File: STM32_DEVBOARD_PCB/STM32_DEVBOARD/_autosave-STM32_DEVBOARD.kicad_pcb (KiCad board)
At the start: 2 copper layers, 49.8 x 40.4 mm, 62 parts, among them J1 Screw_Terminal_01x02, J2 USB_C_Receptacle_USB2.0, J3 SWD, J4 Conn_01x03_Pin, Q1 AO3401A, SW1 BTN_RSET, SW2 BTN1, U1 USBLC6-2P6, U2 TPMP2359DJ, U3 STM32F401RCTx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

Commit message: Added images and more tidy of PCB
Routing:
- net GND: track 92.7 -> 94.3 mm, vias 25 -> 26
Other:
- board text added: "CLK"
- board text added: "IO"
- board text added: "O"
- board text added: "RST"
- board text removed: "SWCLK"
- board text removed: "SWDIO"
- board text removed: "SWO"
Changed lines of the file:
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@@
       (rotate (xyz 0 0 0))
     )
+    (model "C:/Users/me/Dropbox/01_PROJECTS/23_STM32_DEVBOAD/STM32_DEVBOARD/STM32_DEVBOARD_PCB/Component Models/USB_HRO_TYPE-C-31-M-12.step"
+      (offset (xyz -4.5 -3.65 0))
+      (scale (xyz 1 1 1))
+      (rotate (xyz 0 0 0))
+    )
   )
   (footprint "Diode_SMD:D_MiniMELF" (layer "F.Cu")
@@
     (property "ki_keywords" "Arm Cortex-M4 STM32F4 STM32F401")
     (attr smd)
-    (fp_text reference "U3" (at 0 -7.4 90) (layer "F.SilkS")
+    (fp_text reference "U3" (at -1.116 -7.51 90) (layer "F.SilkS")
         (effects (font (size 1 1) (thickness 0.15)))
     )
@@
     (effects (font (size 1 1) (thickness 0.15)) (justify left bottom))
   )
-  (gr_text "SWDIO" (at 151.7396 101.8032) (layer "F.SilkS")
-    (effects (font (size 0.5 0.5) (thickness 0.125)) (justify left bottom))
+  (gr_text "IO" (at 152.4 102.108) (layer "F.SilkS")
+    (effects (font (size 1 1) (thickness 0.125)) (justify left bottom))
   )
-  (gr_text "GND" (at 160.8328 100.6856) (layer "F.SilkS")
-    (effects (font (size 0.5 0.5) (thickness 0.125)) (justify left bottom))
+  (gr_text "GND" (at 160.782 100.838) (layer "F.SilkS")
+    (effects (font (size 1 1) (thickness 0.125)) (justify left bottom))
   )
   (gr_text "USRBTN" (at 128.651 77.1652) (layer "F.SilkS")
     (effects (font (size 0.5 0.5) (thickness 0.125)) (justify bottom))
   )
-  (gr_text "BOOT0" (at 144.4244 107.442 90) (layer "F.SilkS")
-    (effects (font (size 0.5 0.5) (thickness 0.125)) (justify right bottom))
+  (gr_text "RST" (at 152.908 96.012) (layer "F.SilkS")
+    (effects (font (size 1 1) (thickness 0.125)) (justify left bottom))
+  )
+  (gr_text "BOOT0" (at 144.526 107.442 90) (layer "F.SilkS")
+    (effects (font (size 1 1) (thickness 0.125)) (justify right bottom))
   )
-  (gr_text "SWO" (at 152.4508 99.3648) (layer "F.SilkS")
-    (effects (font (size 0.5 0.5) (thickness 0.125)) (justify left bottom))
+  (gr_text "O" (at 152.908 99.568) (layer "F.SilkS")
+    (effects (font (size 1 1) (thickness 0.125)) (justify left bottom))
   )
-  (gr_text "GND" (at 145.6944 107.442 90) (layer "F.SilkS")
-    (effects (font (size 0.5 0.5) (thickness 0.125)) (justify right bottom))
+  (gr_text "GND" (at 146.05 107.442 90) (layer "F.SilkS")
+    (effects (font (size 1 1) (thickness 0.125)) (justify right bottom))
   )
-  (gr_text "3.3V" (at 143.1544 107.442 90) (layer "F.SilkS")
-    (effects (font (size 0.5 0.5) (thickness 0.125)) (justify right bottom))
+  (gr_text "3.3V" (at 143.256 107.442 90) (layer "F.SilkS")
+    (effects (font (size 1 1) (thickness 0.125)) (justify right bottom))
   )
-  (gr_text "SWCLK" (at 151.5872 100.6348) (layer "F.SilkS")
-    (effects (font (size 0.5 0.5) (thickness 0.125)) (justify left bottom))
+  (gr_text "CLK" (at 151.13 100.838) (layer "F.SilkS")
+    (effects (font (size 1 1) (thickness 0.125)) (justify left bottom))
   )
   (gr_text "RESET" (at 138.938 77.1652) (layer "F.SilkS")
     (effects (font (size 0.5 0.5) (thickness 0.125)) (justify bottom))
   )
-  (gr_text "3.3V" (at 160.8328 101.9048) (layer "F.SilkS")
-    (effects (font (size 0.5 0.5) (thickness 0.125)) (justify left bottom))
+  (gr_text "3.3V" (at 160.8328 102.108) (layer "F.SilkS")
+    (effects (font (size 1 1) (thickness 0.125)) (justify left bottom))
   )
   (gr_text "0V" (at 136.2456 115.189) (layer "F.SilkS")
@@
   (segment (start 151.835 90.83) (end 150.266 90.83) (width 0.3) (layer "F.Cu") (net 2))
   (segment (start 159.516 93.5995) (end 160.516 93.5995) (width 0.25) (layer "F.Cu") (net 2))
+  (segment (start 137.414 100.304218) (end 138.442891 101.333109) (width 0.3) (layer "F.Cu") (net 2))
   (segment (start 144.41 88.405) (end 144.41 86.984) (width 0.3) (layer "F.Cu") (net 2))
   (segment (start 138.811 97.183) (end 138.958 97.33) (width 0.3) (layer "F.Cu") (net 2))
@@
   (segment (start 149.354 104.265) (end 148.844 104.775) (width 0.25) (layer "F.Cu") (net 2))
   (segment (start 148.577 78.327) (end 148.252 78.652) (width 0.5) (layer "F.Cu") (net 2))
+  (segment (start 137.414 100.076) (end 137.414 100.304218) (width 0.3) (layer "F.Cu") (net 2))
   (segment (start 137.401 82.931) (end 136.017 82.931) (width 0.3) (layer "F.Cu") (net 2))
   (segment (start 155.577 106.426) (end 156.21 106.426) (width 0.5) (layer "F.Cu") (net 2))
@@
   (via (at 156.21 83.82) (size 0.8) (drill 0.4) (layers "F.Cu" "B.Cu") (net 2))
   (via (at 124.46 100.965) (size 0.8) (drill 0.4) (layers "F.Cu" "B.Cu") (net 2))
+  (via (at 138.442891 101.333109) (size 0.8) (drill 0.4) (layers "F.Cu" "B.Cu") (net 2))
   (via (at 157.3784 100.33) (size 0.8) (drill 0.4) (layers "F.Cu" "B.Cu") (net 2))
   (via (at 151.384 82.169) (size 0.8) (drill 0.4) (layers "F.Cu" "B.Cu") (net 2))

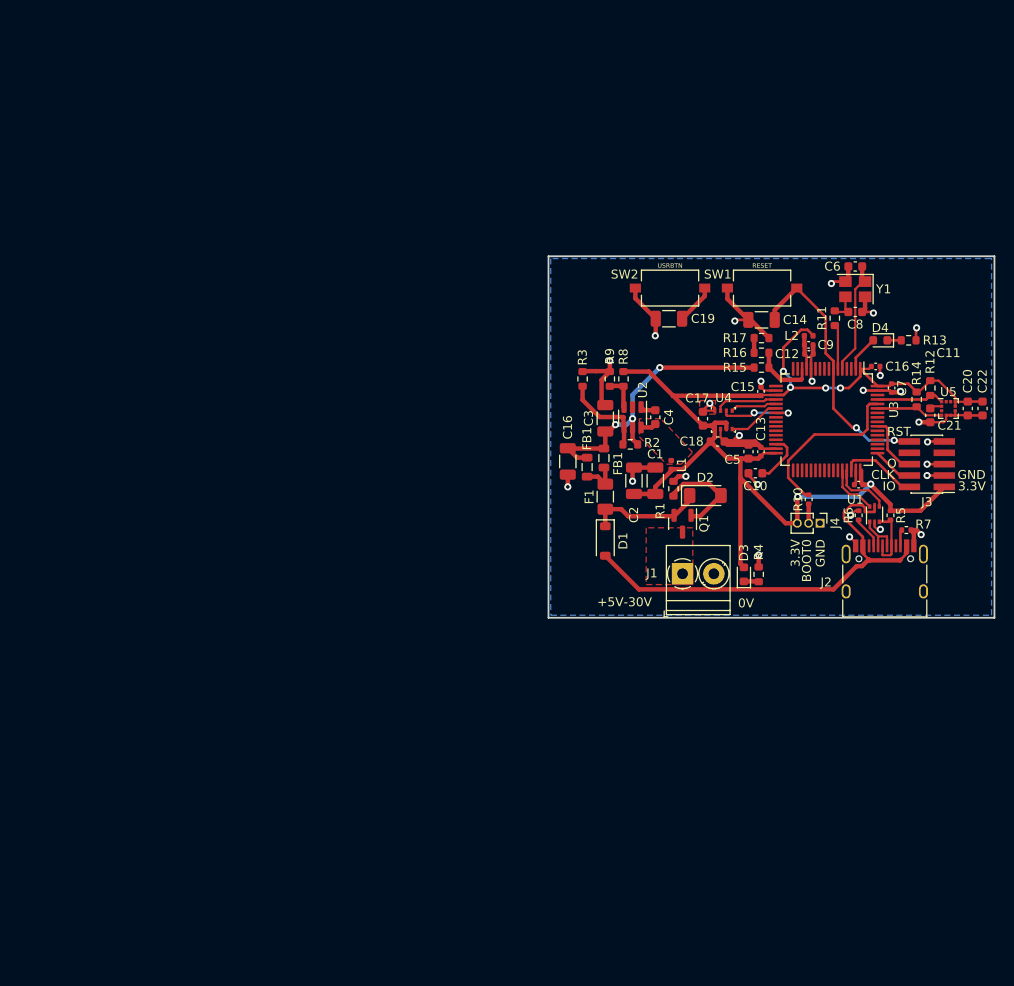
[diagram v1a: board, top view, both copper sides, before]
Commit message: Added images of render
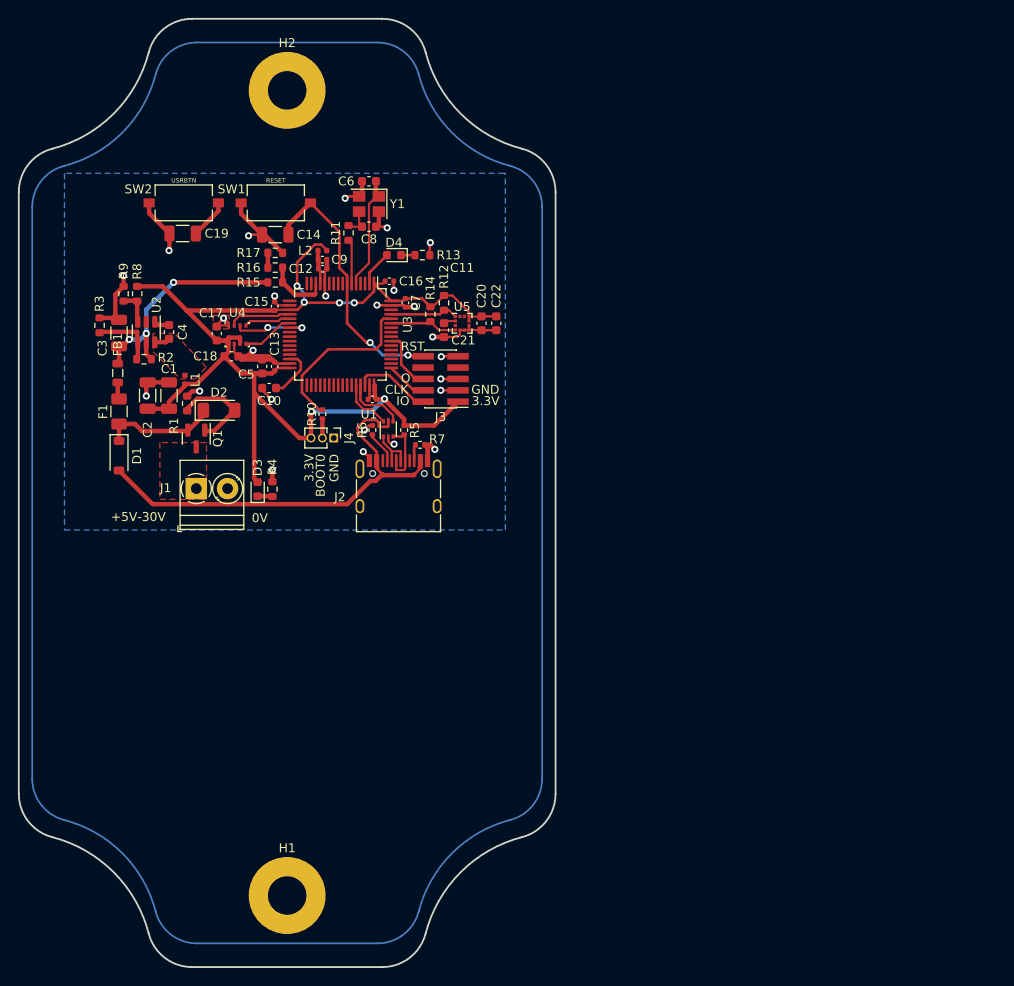
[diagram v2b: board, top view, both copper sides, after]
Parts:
- removed the C16 at (117.2, 98.8)
- removed the FB1 at (121.3, 98.4)
- added H1: MountingHole, MountingHole:MountingHole_4.3mm_M4_Pad, F.Cu at (85.9, 147.3)
- added H2: MountingHole, MountingHole:MountingHole_4.3mm_M4_Pad, F.Cu at (85.9, 57.3)
- moved C11 55.2 mm to (95.4, 91.8)
- moved C12 55.2 mm to (89.8, 77.2)
- moved C13 55.2 mm to (84.5, 88.1)
- moved C14 55.2 mm to (84.5, 73.4)
- moved C15 55.2 mm to (84.5, 81.4)
- moved C16 55.2 mm to (97.3, 78.6)
- moved C17 55.2 mm to (78.0, 84.5)
- moved C20 55.2 mm to (107.6, 83.3)
- moved C22 55.2 mm to (109.2, 83.3)
- moved C3 55.2 mm to (67.1, 84.4)
- moved C6 55.2 mm to (95.0, 67.4)
- moved C8 55.2 mm to (95.0, 72.5)
- moved C9 55.2 mm to (89.8, 76.2)
- moved D1 55.2 mm to (67.1, 98.1)
- moved D3 55.2 mm to (82.5, 101.9)
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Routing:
- net BUCK_IN: track 33.1 -> 26.3 mm
- net BUCK_EN: track 10.1 -> 7.39 mm
- net Net-(F1-Pad1): track 4.24 -> 1.89 mm
- net GND: track 94.3 -> 92.2 mm, vias 26 -> 25
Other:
- board size 49.8 x 40.4 mm -> 60 x 106 mm
